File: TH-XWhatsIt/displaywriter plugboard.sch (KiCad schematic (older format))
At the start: 3 parts, among them J10 DISPLAYWRITER PLUGBOARD CONNE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, J11 DISPLAYWRITER PLUGBOARD ROWS, J9 DISPLAYWRITER PLUGBOARD COLUM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

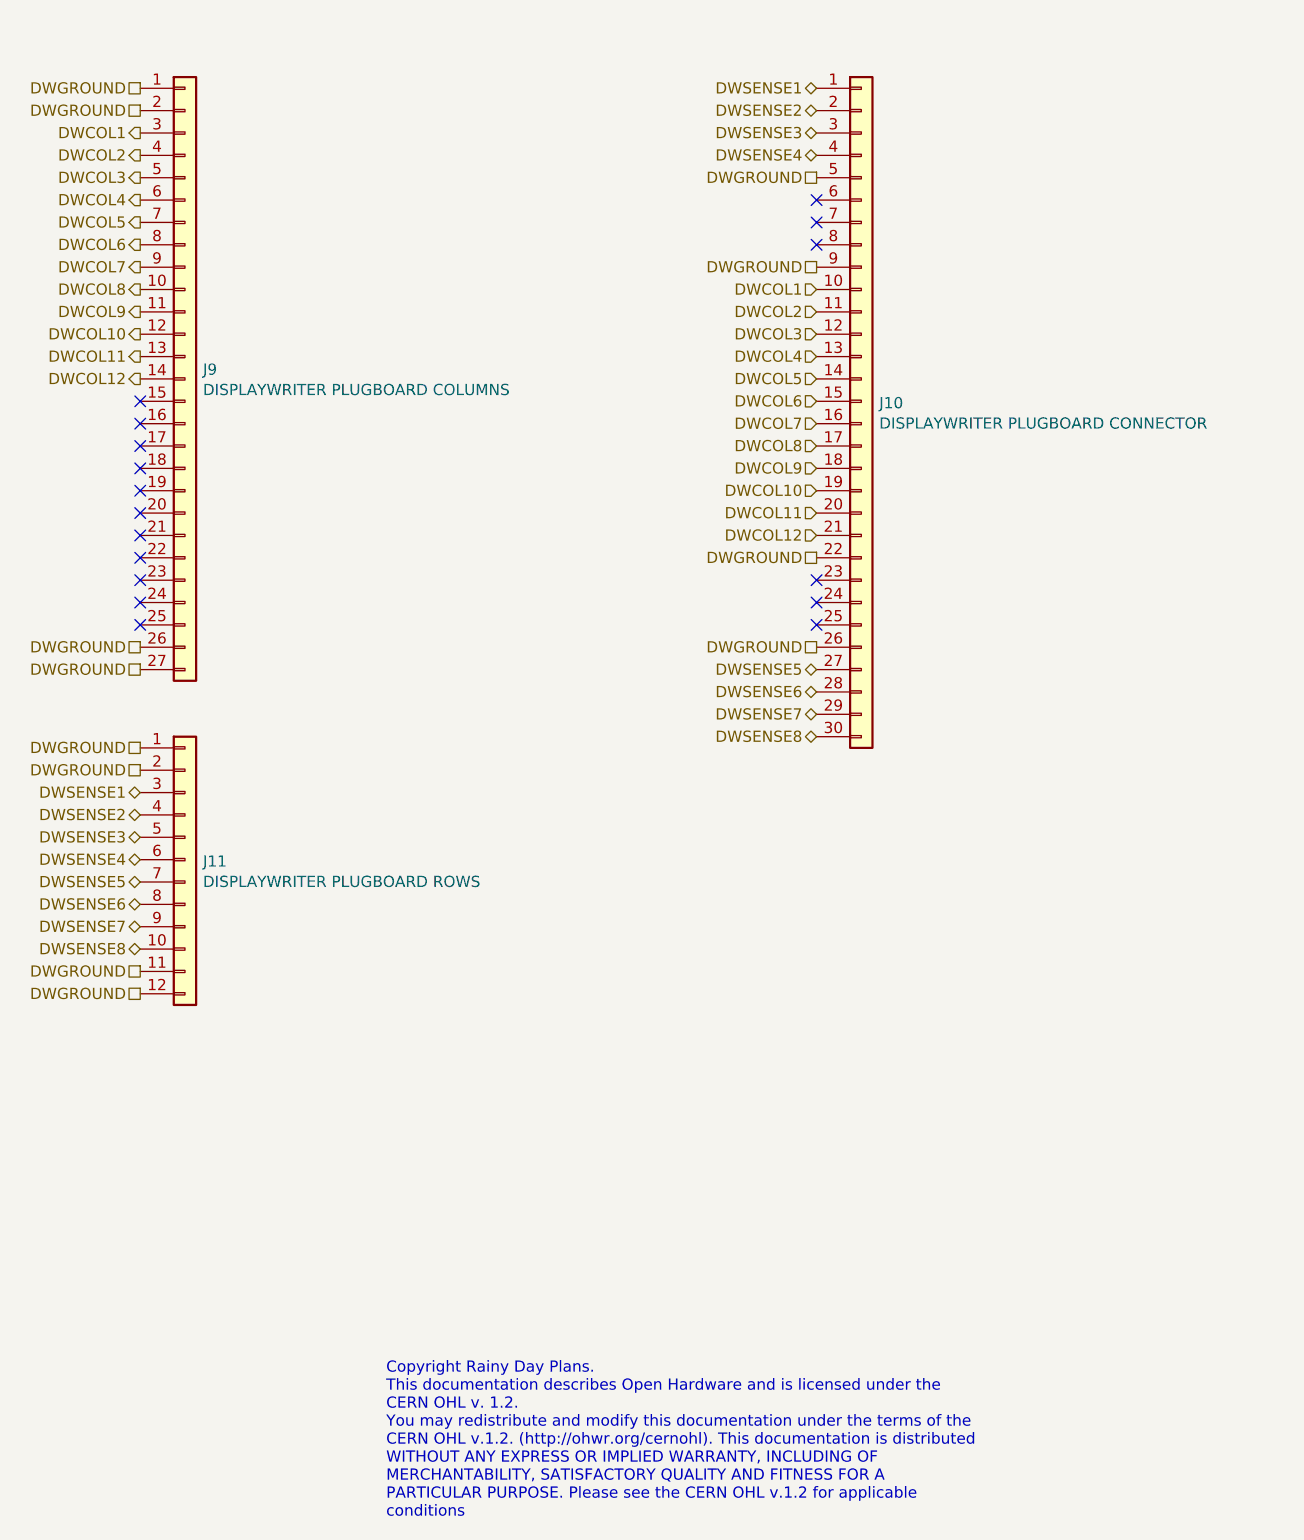
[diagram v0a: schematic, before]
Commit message: version bump to 2.0 due to header position changes finished wiring up most of the plugboards, but displaywriter as per usual is the most annoying.....see changes file for more details (jan 3rd, 2020)
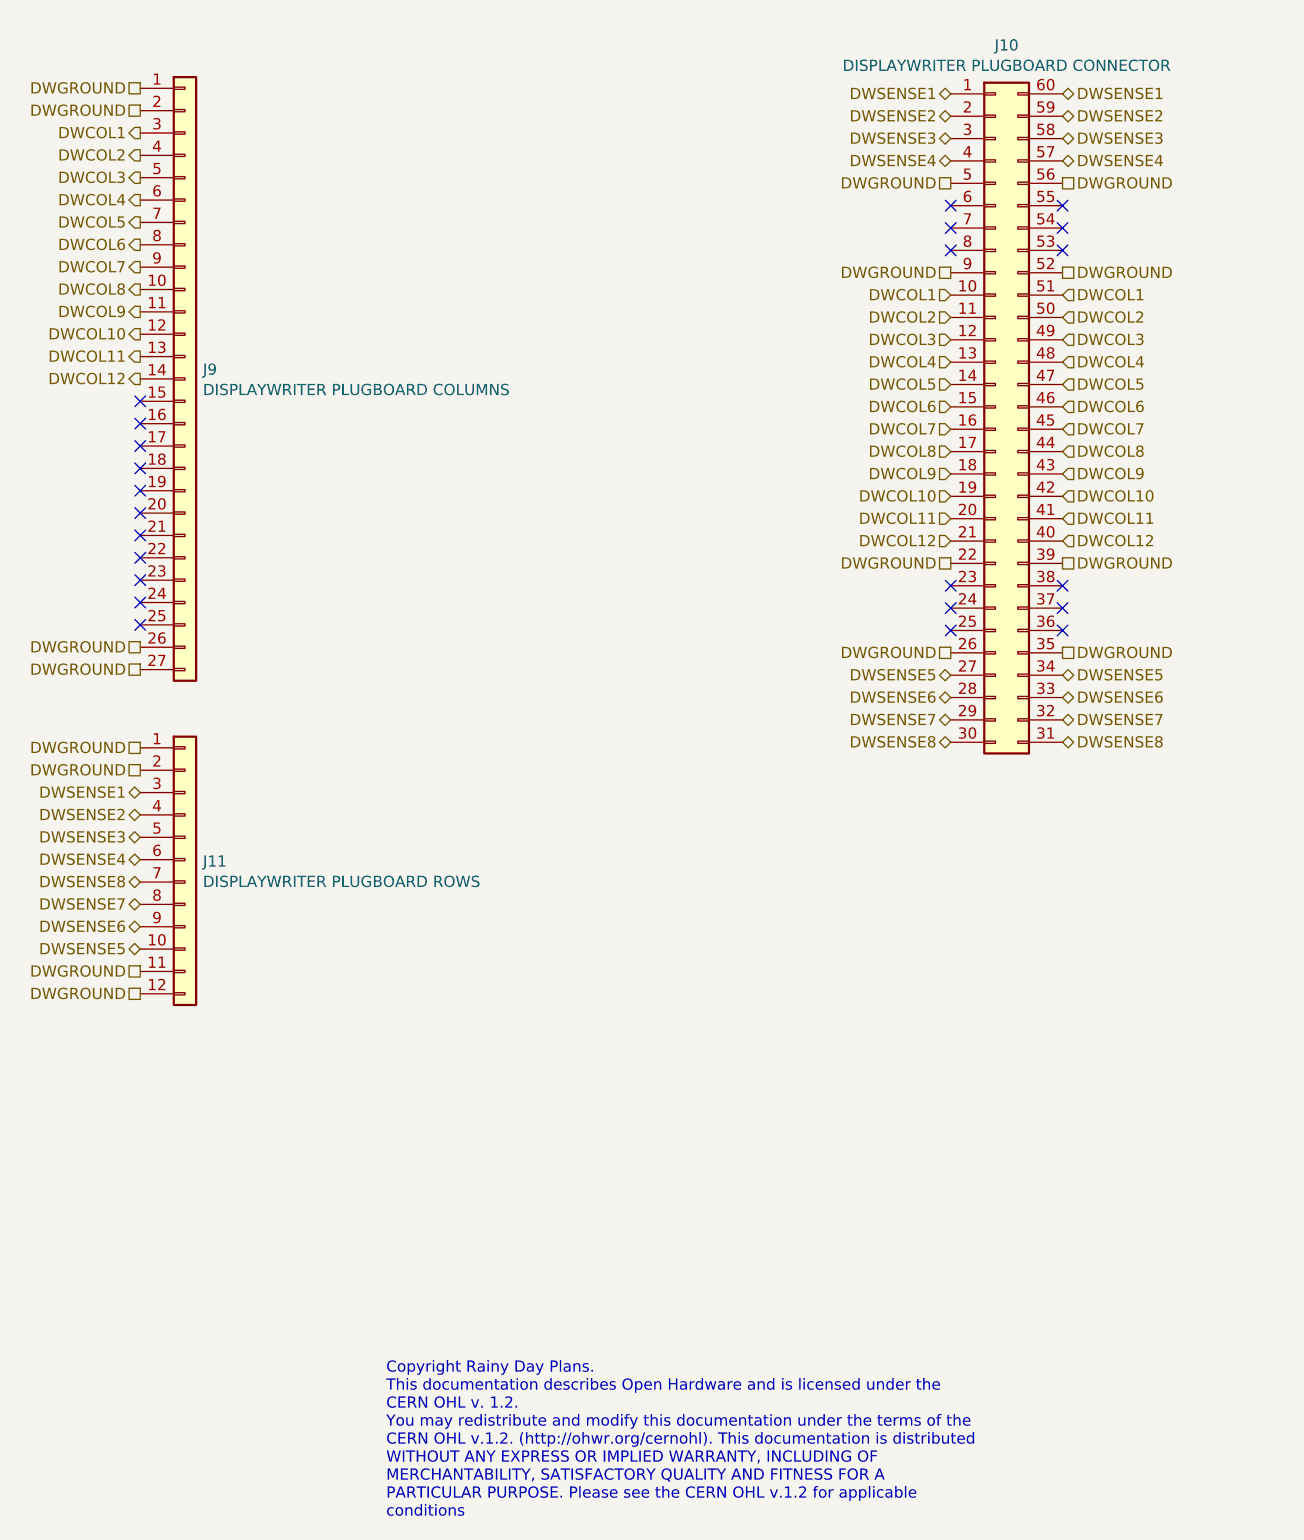
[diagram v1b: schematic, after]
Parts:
- removed J10: DISPLAYWRITER PLUGBOARD CONNECTOR, TH-XWhatsIt:3..6mm_cardedge, symbol Connector_Generic:Conn_01x30
- added J10: DISPLAYWRITER PLUGBOARD CONNECTOR, TH-XWhatsIt:DIP-60_155_ELL, symbol Connector_Generic:Conn_02x30_Counter_Clockwise
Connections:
- net DWCOL1: now also J10.10 (Pin_10), J10.51 (Pin_51)
- net DWCOL10: now also J10.19 (Pin_19), J10.42 (Pin_42)
- net DWCOL11: now also J10.20 (Pin_20), J10.41 (Pin_41)
- net DWCOL12: now also J10.21 (Pin_21), J10.40 (Pin_40)
- net DWCOL2: now also J10.11 (Pin_11), J10.50 (Pin_50)
- net DWCOL3: now also J10.12 (Pin_12), J10.49 (Pin_49)
- net DWCOL4: now also J10.13 (Pin_13), J10.48 (Pin_48)
- net DWCOL5: now also J10.14 (Pin_14), J10.47 (Pin_47)
- net DWCOL6: now also J10.15 (Pin_15), J10.46 (Pin_46)
- net DWCOL7: now also J10.16 (Pin_16), J10.45 (Pin_45)
- net DWCOL8: now also J10.17 (Pin_17), J10.44 (Pin_44)
- net DWCOL9: now also J10.18 (Pin_18), J10.43 (Pin_43)
- net DWGROUND: now also J10.22 (Pin_22), J10.26 (Pin_26), J10.35 (Pin_35), J10.39 (Pin_39), J10.5 (Pin_5), J10.52 (Pin_52), J10.56 (Pin_56), J10.9 (Pin_9)
- net DWSENSE1: now also J10.1 (Pin_1), J10.60 (Pin_60)
- net DWSENSE2: now also J10.2 (Pin_2), J10.59 (Pin_59)
- net DWSENSE3: now also J10.3 (Pin_3), J10.58 (Pin_58)
- net DWSENSE4: now also J10.4 (Pin_4), J10.57 (Pin_57)
- net DWSENSE5: now also J11.10 (Pin_10), J10.27 (Pin_27), J10.34 (Pin_34); no longer J11.7 (Pin_7)
- net DWSENSE6: now also J11.9 (Pin_9), J10.28 (Pin_28), J10.33 (Pin_33); no longer J11.8 (Pin_8)
- net DWSENSE7: now also J11.8 (Pin_8), J10.29 (Pin_29), J10.32 (Pin_32); no longer J11.9 (Pin_9)
- net DWSENSE8: now also J11.7 (Pin_7), J10.30 (Pin_30), J10.31 (Pin_31); no longer J11.10 (Pin_10)
- no-connect marks 17 -> 23
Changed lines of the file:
@@
 EESchema Schematic File Version 4
+LIBS:TH-XWhatsIt-cache
 EELAYER 30 0
 EELAYER END
@@
 Title "Displaywriter plugboard to convert controller signals"
 Date "2020-01-31"
-Rev "0.01"
+Rev "0.0.2"
 Comp "Rainy Day Plans"
 Comment1 ""
@@
 	1    0    0    -1
 $EndComp
-$Comp
-L Connector_Generic:Conn_01x30 J10
-U 1 1 5E9BABE3
-P 6075 2750
-F 0 "J10" H 6155 2742 50  0000 L CNN
-F 1 "DISPLAYWRITER PLUGBOARD CONNECTOR" H 6155 2651 50  0000 L CNN
-F 2 "TH-XWhatsIt:3..6mm_cardedge" H 6075 2750 50  0001 C CNN
-F 3 "~" H 6075 2750 50  0001 C CNN
-	1    6075 2750
-	1    0    0    -1
-$EndComp
-NoConn ~ 5875 3550
-NoConn ~ 5875 3650
-NoConn ~ 5875 3750
-NoConn ~ 5875 1850
-NoConn ~ 5875 1950
-NoConn ~ 5875 2050
+NoConn ~ 6475 3575
+NoConn ~ 6475 3675
+NoConn ~ 6475 3775
+NoConn ~ 6475 1875
+NoConn ~ 6475 1975
+NoConn ~ 6475 2075
 Text HLabel 2850 1550 0    50   Output ~ 0
 DWCOL1
@@
 Text HLabel 2850 4800 0    50   BiDi ~ 0
 DWSENSE4
+Text HLabel 2850 5200 0    50   BiDi ~ 0
+DWSENSE5
+Text HLabel 2850 5100 0    50   BiDi ~ 0
+DWSENSE6
+Text HLabel 2850 5000 0    50   BiDi ~ 0
+DWSENSE7
 Text HLabel 2850 4900 0    50   BiDi ~ 0
+DWSENSE8
+Text HLabel 6475 1375 0    50   BiDi ~ 0
+DWSENSE1
+Text HLabel 6475 1475 0    50   BiDi ~ 0
+DWSENSE2
+Text HLabel 6475 1575 0    50   BiDi ~ 0
+DWSENSE3
+Text HLabel 6475 1675 0    50   BiDi ~ 0
+DWSENSE4
+Text HLabel 6475 3975 0    50   BiDi ~ 0
 DWSENSE5
-Text HLabel 2850 5000 0    50   BiDi ~ 0
+Text HLabel 6475 4075 0    50   BiDi ~ 0
 DWSENSE6
-Text HLabel 2850 5100 0    50   BiDi ~ 0
+Text HLabel 6475 4175 0    50   BiDi ~ 0
 DWSENSE7
-Text HLabel 2850 5200 0    50   BiDi ~ 0
+Text HLabel 6475 4275 0    50   BiDi ~ 0
 DWSENSE8
-Text HLabel 5875 1350 0    50   BiDi ~ 0
-DWSENSE1
-Text HLabel 5875 1450 0    50   BiDi ~ 0
-DWSENSE2
-Text HLabel 5875 1550 0    50   BiDi ~ 0
-DWSENSE3
-Text HLabel 5875 1650 0    50   BiDi ~ 0
-DWSENSE4
-Text HLabel 5875 3950 0    50   BiDi ~ 0
-DWSENSE5
-Text HLabel 5875 4050 0    50   BiDi ~ 0
-DWSENSE6
-Text HLabel 5875 4150 0    50   BiDi ~ 0
-DWSENSE7
-Text HLabel 5875 4250 0    50   BiDi ~ 0
-DWSENSE8
-Text HLabel 5875 2250 0    50   Input ~ 0
+Text HLabel 6475 2275 0    50   Input ~ 0
 DWCOL1
-Text HLabel 5875 2350 0    50   Input ~ 0
+Text HLabel 6475 2375 0    50   Input ~ 0
 DWCOL2
-Text HLabel 5875 2450 0    50   Input ~ 0
+Text HLabel 6475 2475 0    50   Input ~ 0
 DWCOL3
-Text HLabel 5875 2550 0    50   Input ~ 0
+Text HLabel 6475 2575 0    50   Input ~ 0
 DWCOL4
-Text HLabel 5875 2650 0    50   Input ~ 0
+Text HLabel 6475 2675 0    50   Input ~ 0
 DWCOL5
-Text HLabel 5875 2750 0    50   Input ~ 0
+Text HLabel 6475 2775 0    50   Input ~ 0
 DWCOL6
-Text HLabel 5875 2850 0    50   Input ~ 0
+Text HLabel 6475 2875 0    50   Input ~ 0
 DWCOL7
-Text HLabel 5875 2950 0    50   Input ~ 0
+Text HLabel 6475 2975 0    50   Input ~ 0
 DWCOL8
-Text HLabel 5875 3050 0    50   Input ~ 0
+Text HLabel 6475 3075 0    50   Input ~ 0
 DWCOL9
-Text HLabel 5875 3150 0    50   Input ~ 0
+Text HLabel 6475 3175 0    50   Input ~ 0
 DWCOL10
-Text HLabel 5875 3250 0    50   Input ~ 0
+Text HLabel 6475 3275 0    50   Input ~ 0
 DWCOL11
-Text HLabel 5875 3350 0    50   Input ~ 0
+Text HLabel 6475 3375 0    50   Input ~ 0
 DWCOL12
 Text HLabel 2850 1350 0    50   UnSpc ~ 0
@@
 Text HLabel 2850 5400 0    50   UnSpc ~ 0
 DWGROUND
-Text HLabel 5875 1750 0    50   UnSpc ~ 0
-DWGROUND
-Text HLabel 5875 2150 0    50   UnSpc ~ 0
-DWGROUND
-Text HLabel 5875 3450 0    50   UnSpc ~ 0
-DWGROUND
-Text HLabel 5875 3850 0    50   UnSpc ~ 0
+Text HLabel 6475 1775 0    50   UnSpc ~ 0
+DWGROUND
+Text HLabel 6475 2175 0    50   UnSpc ~ 0
+DWGROUND
+Text HLabel 6475 3475 0    50   UnSpc ~ 0
+DWGROUND
+Text HLabel 6475 3875 0    50   UnSpc ~ 0
 DWGROUND
 NoConn ~ 2850 2750
@@
 Text Notes 3950 7750 0    50   ~ 0
 Copyright Rainy Day Plans.\nThis documentation describes Open Hardware and is licensed under the\nCERN OHL v. 1.2.\nYou may redistribute and modify this documentation under the terms of the\nCERN OHL v.1.2. (http://ohwr.org/cernohl). This documentation is distributed\nWITHOUT ANY EXPRESS OR IMPLIED WARRANTY, INCLUDING OF\nMERCHANTABILITY, SATISFACTORY QUALITY AND FITNESS FOR A\nPARTICULAR PURPOSE. Please see the CERN OHL v.1.2 for applicable\nconditions
+$Comp
+L Connector_Generic:Conn_02x30_Counter_Clockwise J10
+U 1 1 5E4284EA
+P 6675 2775
+F 0 "J10" H 6725 4392 50  0000 C CNN
+F 1 "DISPLAYWRITER PLUGBOARD CONNECTOR" H 6725 4301 50  0000 C CNN
+F 2 "TH-XWhatsIt:DIP-60_155_ELL" H 6675 2775 50  0001 C CNN
+F 3 "~" H 6675 2775 50  0001 C CNN
+	1    6675 2775
+	1    0    0    -1
+$EndComp
+NoConn ~ 6975 3575
+NoConn ~ 6975 3675
+NoConn ~ 6975 3775
+NoConn ~ 6975 1875
+NoConn ~ 6975 1975
+NoConn ~ 6975 2075
+Text HLabel 6975 1375 2    50   BiDi ~ 0
+DWSENSE1
+Text HLabel 6975 1475 2    50   BiDi ~ 0
+DWSENSE2
+Text HLabel 6975 1575 2    50   BiDi ~ 0
+DWSENSE3
+Text HLabel 6975 1675 2    50   BiDi ~ 0
+DWSENSE4
+Text HLabel 6975 3975 2    50   BiDi ~ 0
+DWSENSE5
+Text HLabel 6975 4075 2    50   BiDi ~ 0
+DWSENSE6
+Text HLabel 6975 4175 2    50   BiDi ~ 0
+DWSENSE7
+Text HLabel 6975 4275 2    50   BiDi ~ 0
+DWSENSE8
+Text HLabel 6975 2275 2    50   Input ~ 0
+DWCOL1
+Text HLabel 6975 2375 2    50   Input ~ 0
+DWCOL2
+Text HLabel 6975 2475 2    50   Input ~ 0
+DWCOL3
+Text HLabel 6975 2575 2    50   Input ~ 0
+DWCOL4
+Text HLabel 6975 2675 2    50   Input ~ 0
+DWCOL5
+Text HLabel 6975 2775 2    50   Input ~ 0
+DWCOL6
+Text HLabel 6975 2875 2    50   Input ~ 0
+DWCOL7
+Text HLabel 6975 2975 2    50   Input ~ 0
+DWCOL8
+Text HLabel 6975 3075 2    50   Input ~ 0
+DWCOL9
+Text HLabel 6975 3175 2    50   Input ~ 0
+DWCOL10
+Text HLabel 6975 3275 2    50   Input ~ 0
+DWCOL11
+Text HLabel 6975 3375 2    50   Input ~ 0
+DWCOL12
+Text HLabel 6975 1775 2    50   UnSpc ~ 0
+DWGROUND
+Text HLabel 6975 2175 2    50   UnSpc ~ 0
+DWGROUND
+Text HLabel 6975 3475 2    50   UnSpc ~ 0
+DWGROUND
+Text HLabel 6975 3875 2    50   UnSpc ~ 0
+DWGROUND
 $EndSCHEMATC

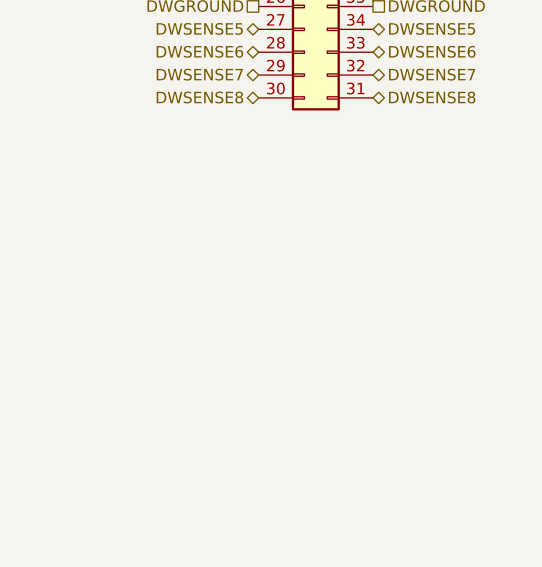
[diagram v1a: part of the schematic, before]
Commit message: finished wiring the dispalywriter plugboard, and added grounding straps to plugboards
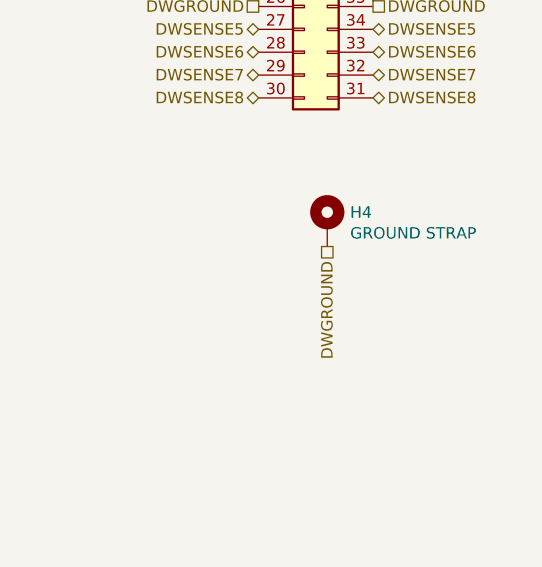
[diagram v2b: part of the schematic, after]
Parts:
- added H4: GROUND STRAP, MountingHole:MountingHole_2.2mm_M2_Pad_Via, symbol Mechanical:MountingHole_Pad
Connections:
- net DWGROUND: now also H4.1
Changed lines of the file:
@@
 Text HLabel 6975 3875 2    50   UnSpc ~ 0
 DWGROUND
+$Comp
+L Mechanical:MountingHole_Pad H4
+U 1 1 5E3A0C5C
+P 6775 4825
+F 0 "H4" H 6875 4874 50  0000 L CNN
+F 1 "GROUND STRAP" H 6875 4783 50  0000 L CNN
+F 2 "MountingHole:MountingHole_2.2mm_M2_Pad_Via" H 6775 4825 50  0001 C CNN
+F 3 "~" H 6775 4825 50  0001 C CNN
+	1    6775 4825
+	1    0    0    -1
+$EndComp
+Text HLabel 6775 4925 3    50   UnSpc ~ 0
+DWGROUND
 $EndSCHEMATC
